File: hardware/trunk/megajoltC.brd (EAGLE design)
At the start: 79.9 x 63 mm, 117 parts, among them IC1 IC_FT230X-SSOP-16, IC2 MCP1826, IC3 MCP1826, J3 JUMPER_CLOSEDTHICK, U1 MCP1700, U11 TLV274, U12 PESDXS4UD, U18 MCP2551SO8, U4 ZXMS6004FF, U8 FAN8303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

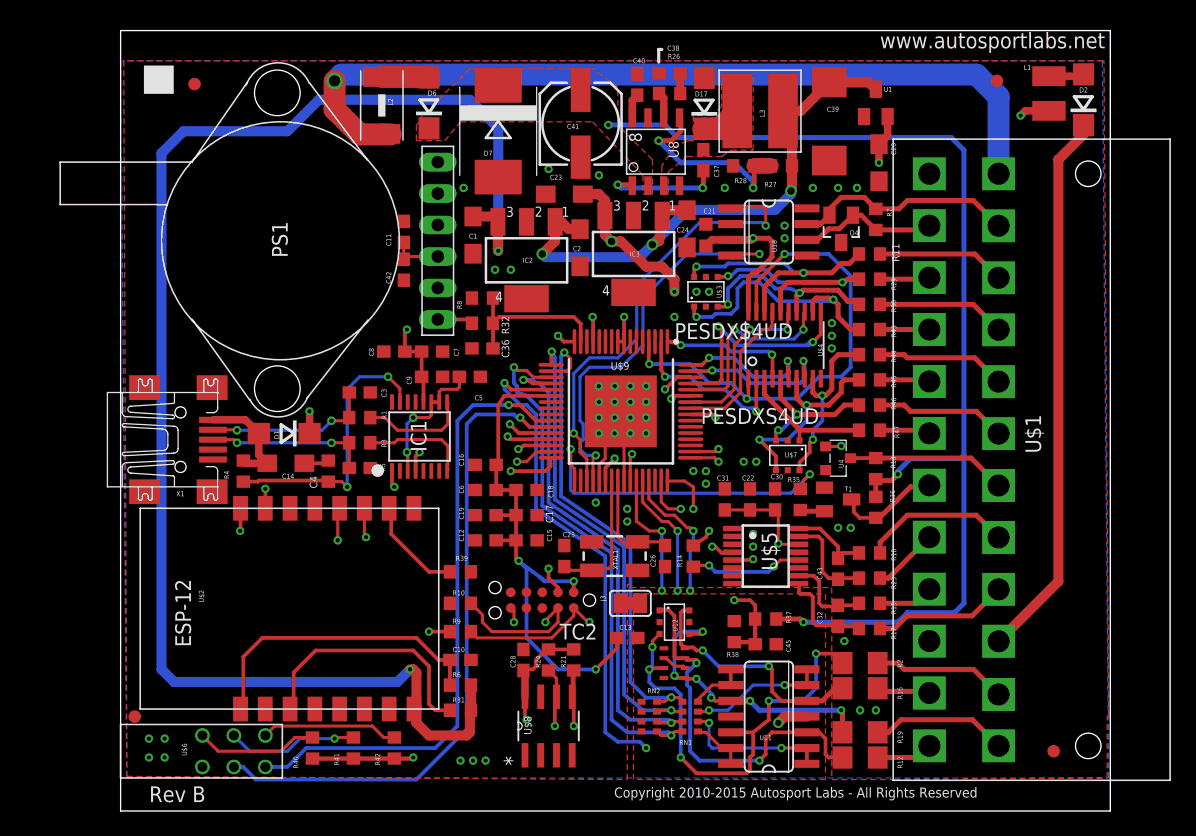
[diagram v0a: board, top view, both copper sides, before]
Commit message: Slight update to routing
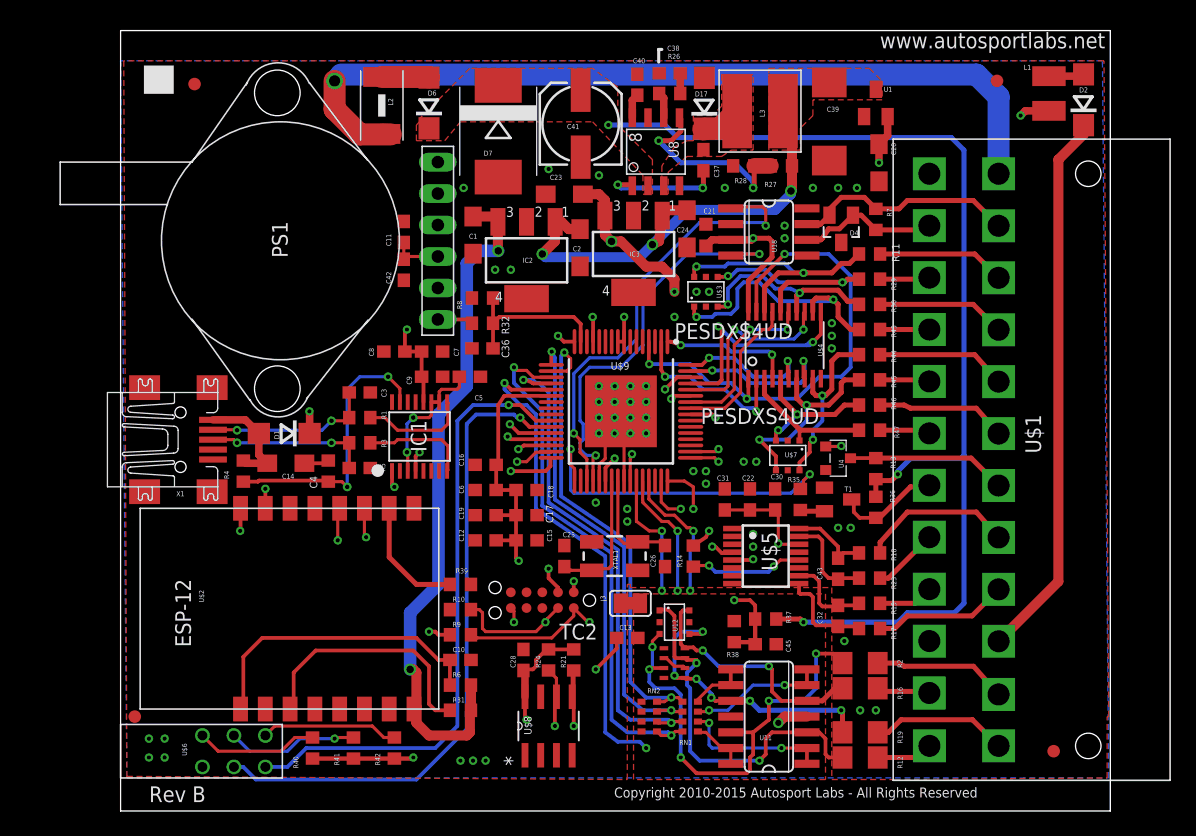
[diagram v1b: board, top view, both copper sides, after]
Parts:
- moved R39 1.02 mm to (27.4, 18.3)
- moved R10 0.51 mm to (27.4, 16.3)
- moved R9 0.25 mm to (27.4, 14.2)
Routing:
- net VCC: track 120.9 -> 56.1 mm
- net +3V3: track 88.5 -> 70.1 mm
- net VDD: track 48.1 -> 39.5 mm
- net SWCLK: track 36.5 -> 34.6 mm
- net N$24: track 8.15 -> 9.76 mm
- added copper zone on layer 1, net VDD

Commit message: Remove R13, minor ground pour changes
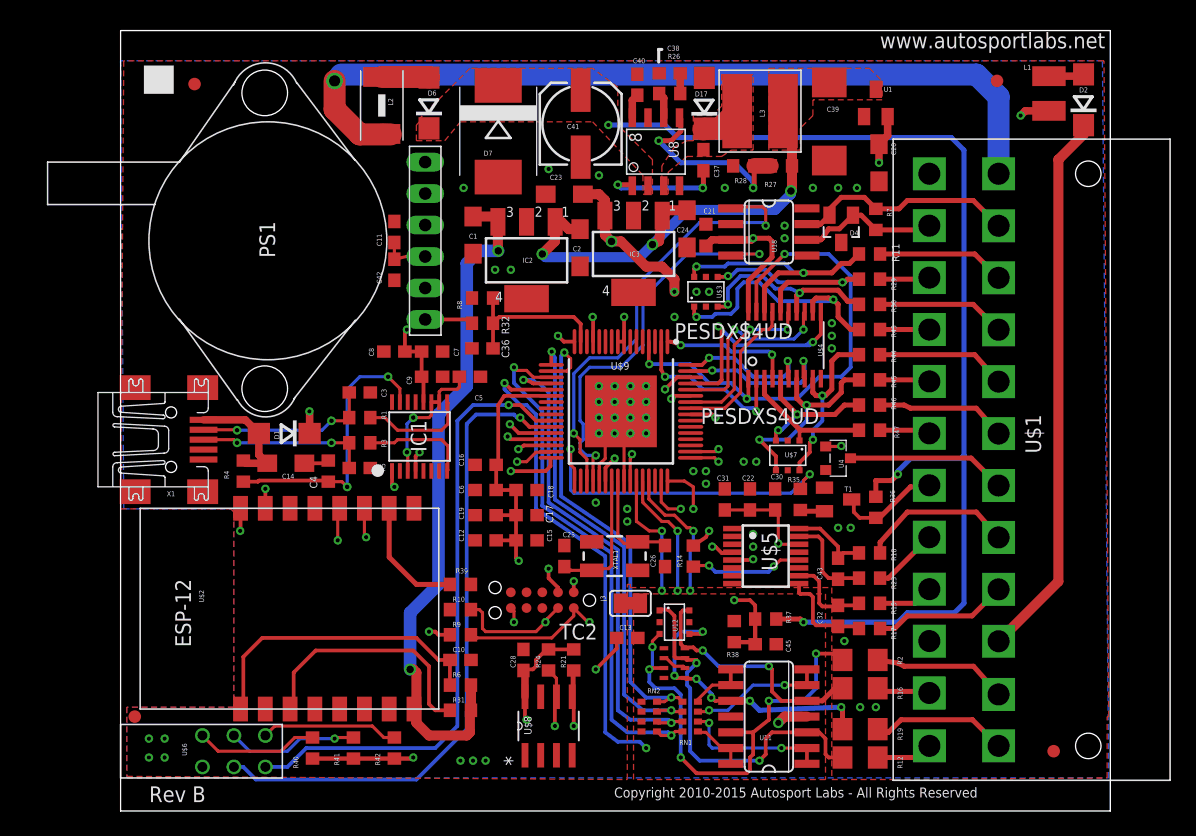
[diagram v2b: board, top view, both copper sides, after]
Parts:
- removed R13: 1K, rcl:R0603
- moved PS1 1.02 mm to (24.6, 46.0)
- moved C11 0.76 mm to (22.1, 46.7)
- moved C42 0.76 mm to (22.1, 43.7)
- moved X1 0.76 mm to (3.17, 30.0)
- moved R19 0.25 mm to (59.7, 6.60)
- moved R2 0.25 mm to (59.7, 12.2)
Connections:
- net PGM_OUT: no longer R13.1
- net SAFE_+12V: no longer R13.2
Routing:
- net N$7: track 2.88 -> 3.90 mm
- net VBUS: track 8.86 -> 9.63 mm
- net FTDI_DP: track 13.1 -> 13.9 mm
- net FTDI_DM: track 13.5 -> 14.2 mm

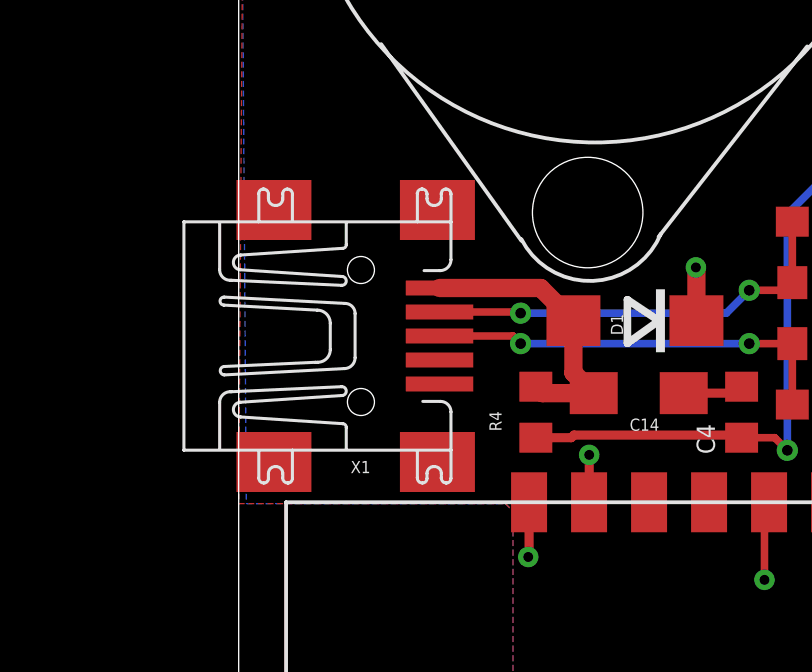
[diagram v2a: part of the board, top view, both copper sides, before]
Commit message: Minor layout trace changes
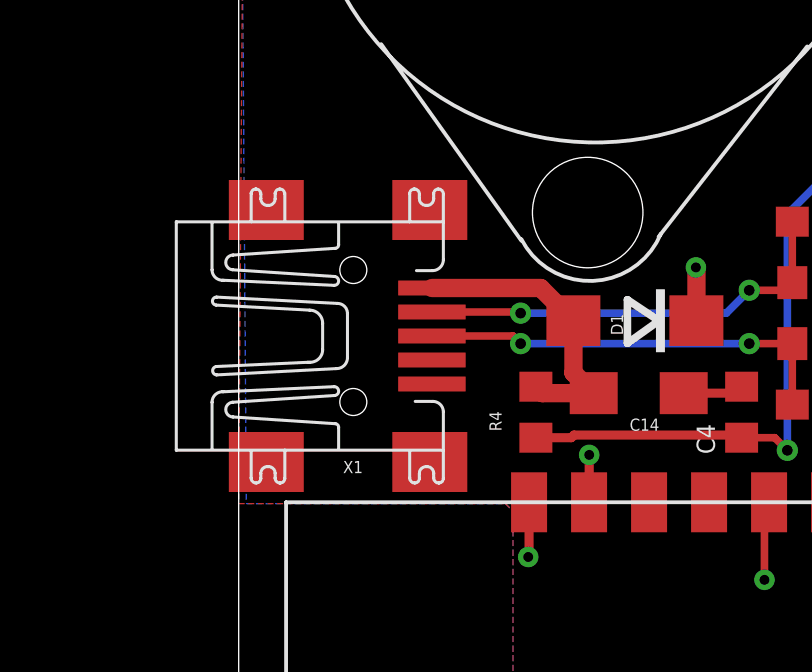
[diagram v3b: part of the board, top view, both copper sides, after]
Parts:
- moved X1 0.25 mm to (2.92, 30.0)
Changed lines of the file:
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@@
 <attribute name="NAME" x="12.811" y="29.999" size="0.4064" layer="25" ratio="10" rot="R90"/>
 </element>
-<element name="X1" library="cnkls_parts" package="MINI-USB_JACK" value="MINI_USB_SHIELD" x="3.175" y="29.972" smashed="yes">
-<attribute name="NAME" x="4.3942" y="25.8064" size="0.4064" layer="25" rot="R180"/>
+<element name="X1" library="cnkls_parts" package="MINI-USB_JACK" value="MINI_USB_SHIELD" x="2.921" y="29.972" smashed="yes">
+<attribute name="NAME" x="4.1402" y="25.8064" size="0.4064" layer="25" rot="R180"/>
 </element>
 <element name="C41" library="rcl" package="153CLV-0605" value="22uF" x="37.1348" y="55.4736" smashed="yes" rot="R90">
@@
 <via x="60.96" y="8.382" extent="1-16" drill="0.3302"/>
 <via x="58.42" y="13.716" extent="1-16" drill="0.3302"/>
-<wire x1="6.695" y1="29.172" x2="6.625" y2="34.172" width="0" layer="19" extent="1-1"/>
+<wire x1="6.441" y1="29.172" x2="6.371" y2="34.172" width="0" layer="19" extent="1-1"/>
 </signal>
 <signal name="+5V">
@@
 <contactref element="X1" pad="1"/>
 <contactref element="R4" pad="2"/>
-<wire x1="6.695" y1="31.572" x2="10.066" y2="31.572" width="0.6096" layer="1"/>
+<wire x1="6.441" y1="31.572" x2="10.066" y2="31.572" width="0.6096" layer="1"/>
 <wire x1="10.066" y1="31.572" x2="11.158" y2="30.48" width="0.6096" layer="1"/>
 <wire x1="11.158" y1="30.48" x2="11.158" y2="28.744" width="0.6096" layer="1"/>
@@
 <contactref element="C3" pad="1"/>
 <wire x1="18.454" y1="33.782" x2="18.454" y2="31.75" width="0.254" layer="1"/>
-<wire x1="6.695" y1="30.772" x2="9.36" y2="30.772" width="0.254" layer="1"/>
+<wire x1="6.441" y1="30.772" x2="9.36" y2="30.772" width="0.254" layer="1"/>
 <wire x1="9.36" y1="30.772" x2="9.398" y2="30.734" width="0.254" layer="1"/>
 <via x="9.398" y="30.734" extent="1-16" drill="0.3556"/>
@@
 <contactref element="C4" pad="1"/>
 <wire x1="18.454" y1="27.686" x2="18.454" y2="29.718" width="0.254" layer="1"/>
-<wire x1="6.695" y1="29.972" x2="9.144" y2="29.972" width="0.254" layer="1"/>
+<wire x1="6.441" y1="29.972" x2="9.144" y2="29.972" width="0.254" layer="1"/>
 <wire x1="9.144" y1="29.972" x2="9.398" y2="29.718" width="0.254" layer="1"/>
 <via x="9.398" y="29.718" extent="1-16" drill="0.3556"/>

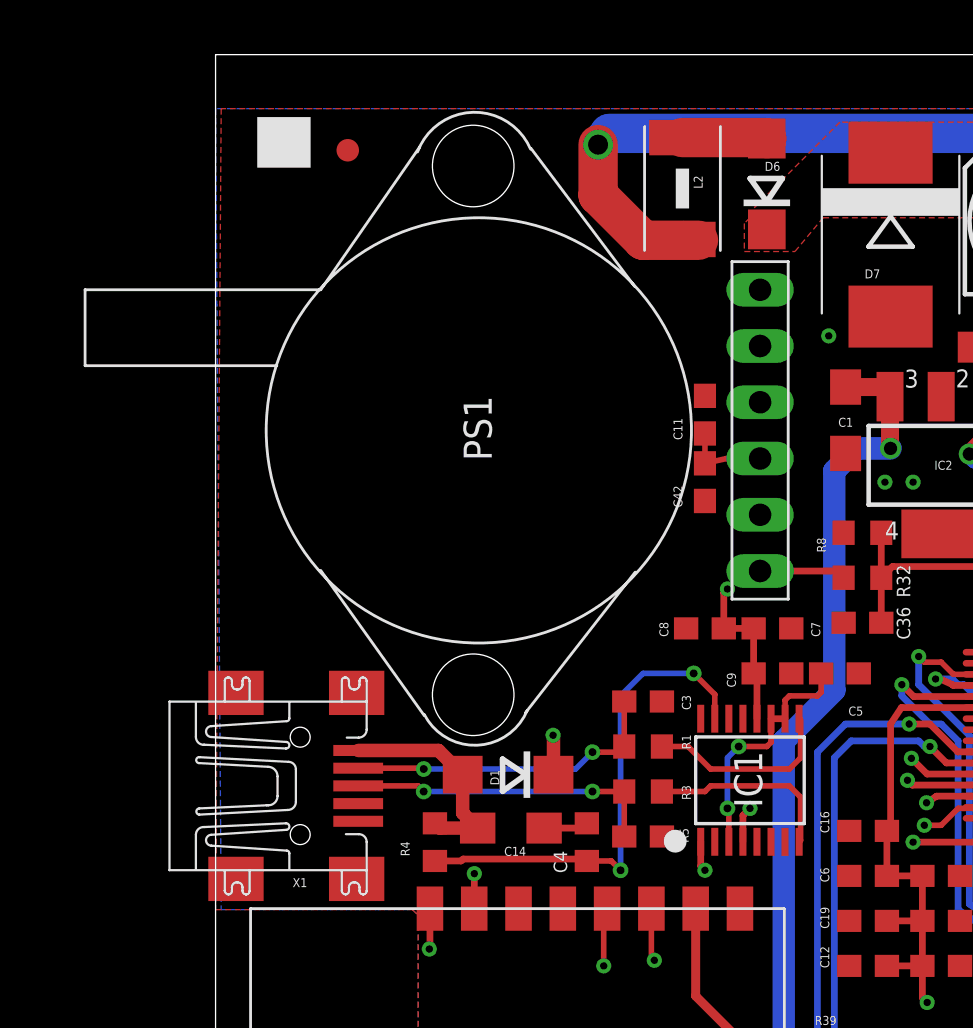
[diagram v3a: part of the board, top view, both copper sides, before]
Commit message: Fix bad ground path issue
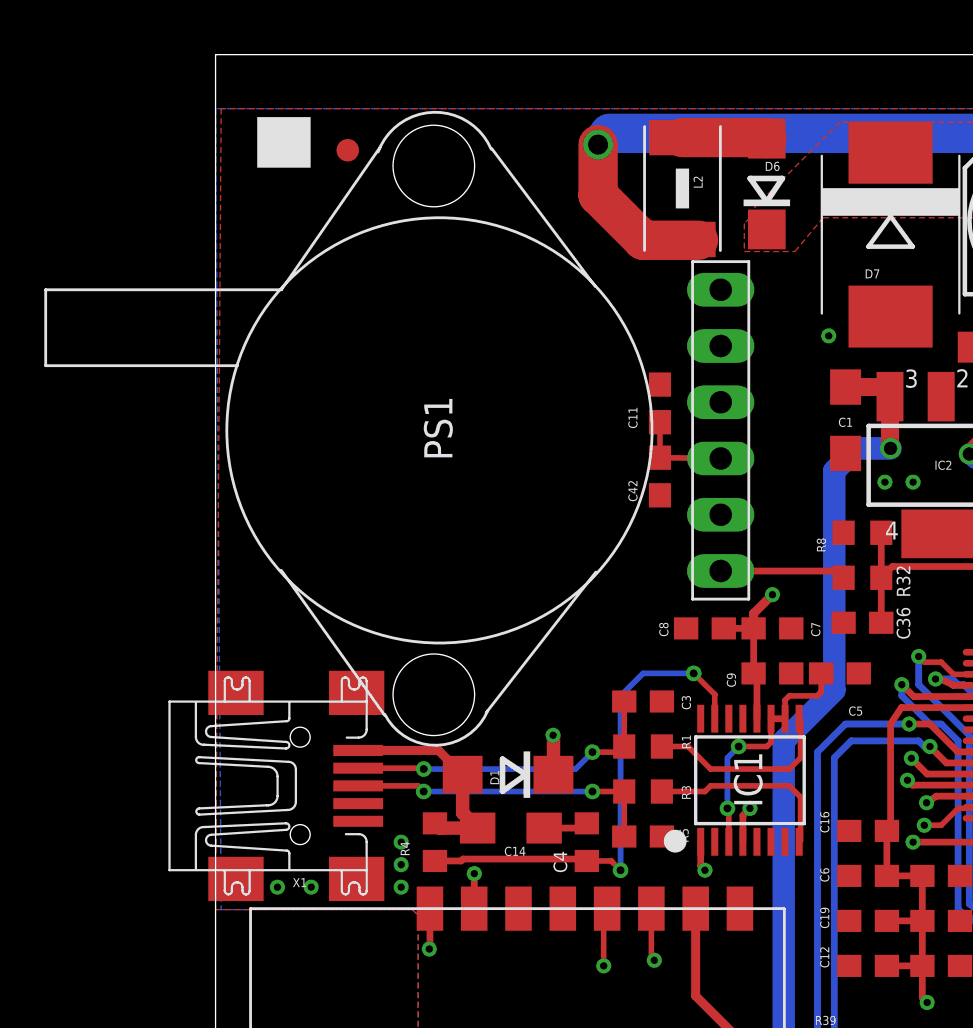
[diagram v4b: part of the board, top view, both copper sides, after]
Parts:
- moved C11 2.09 mm to (20.1, 47.2)
- moved C42 2.05 mm to (20.1, 43.9)
- moved PS1 1.78 mm to (22.8, 46.0)
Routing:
- net N$7: track 3.90 -> 5.68 mm
- net +5V: track 46.0 -> 47.0 mm
- net GND: vias 53 -> 58
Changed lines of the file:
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@@
 <attribute name="NAME" x="58.3694" y="27.6862" size="0.4064" layer="25" rot="R90"/>
 </element>
-<element name="PS1" library="pressure_sensor" package="MPX4250" value="MPX4250" x="24.5872" y="46.0248" smashed="yes" rot="R270">
-<attribute name="NAME" x="12.4714" y="44.6532" size="1.27" layer="25" rot="R90"/>
+<element name="PS1" library="pressure_sensor" package="MPX4250" value="MPX4250" x="22.8092" y="46.0248" smashed="yes" rot="R270">
+<attribute name="NAME" x="10.6934" y="44.6532" size="1.27" layer="25" rot="R90"/>
 </element>
 <element name="R32" library="rcl" package="R0603" value="5.6k" x="29.21" y="39.37" smashed="yes">
@@
 <attribute name="NAME" x="31.369" y="36.576" size="0.6096" layer="25" rot="R90"/>
 </element>
-<element name="C42" library="rcl" package="C0603" value="0.1uf" x="22.098" y="43.688" smashed="yes" rot="R270">
-<attribute name="NAME" x="21.082" y="42.545" size="0.4064" layer="25" rot="R90"/>
+<element name="C42" library="rcl" package="C0603" value="0.1uf" x="20.066" y="43.942" smashed="yes" rot="R270">
+<attribute name="NAME" x="19.05" y="42.799" size="0.4064" layer="25" rot="R90"/>
 </element>
 <element name="T1" library="transistor" package="SOT23-EBC" value="" x="57.912" y="25.146" smashed="yes" rot="R270">
@@
 <attribute name="VALUE" x="59.563" y="28.702" size="1.27" layer="27"/>
 </element>
-<element name="C11" library="rcl" package="C0603" value="0.1uf" x="22.098" y="46.736" smashed="yes" rot="R90">
-<attribute name="NAME" x="21.082" y="45.593" size="0.4064" layer="25" rot="R90"/>
-<attribute name="VALUE" x="24.13" y="45.847" size="1.27" layer="27" rot="R90"/>
+<element name="C11" library="rcl" package="C0603" value="0.1uf" x="20.066" y="47.244" smashed="yes" rot="R90">
+<attribute name="NAME" x="19.05" y="46.101" size="0.4064" layer="25" rot="R90"/>
+<attribute name="VALUE" x="22.098" y="46.355" size="1.27" layer="27" rot="R90"/>
 </element>
 <element name="C6" library="resistor" package="C0603" value="4.7uF" x="29.464" y="25.908" smashed="yes" rot="R180">
@@
 <via x="60.96" y="8.382" extent="1-16" drill="0.3302"/>
 <via x="58.42" y="13.716" extent="1-16" drill="0.3302"/>
-<wire x1="6.441" y1="29.172" x2="6.371" y2="34.172" width="0" layer="19" extent="1-1"/>
+<via x="2.794" y="25.4" extent="1-16" drill="0.3302"/>
+<via x="4.318" y="25.4" extent="1-16" drill="0.3302"/>
+<via x="8.382" y="25.4" extent="1-16" drill="0.3302"/>
+<via x="8.382" y="26.416" extent="1-16" drill="0.3302"/>
+<via x="8.382" y="27.432" extent="1-16" drill="0.3302"/>
 </signal>
 <signal name="+5V">
@@
 <contactref element="C23" pad="+"/>
 <contactref element="L1" pad="1"/>
-<wire x1="24.5872" y1="44.7548" x2="23.0768" y2="44.7548" width="0.254" layer="1"/>
-<wire x1="23.0768" y1="44.7548" x2="22.098" y2="44.538" width="0.254" layer="1"/>
-<wire x1="22.098" y1="44.538" x2="22.098" y2="45.886" width="0.254" layer="1"/>
+<wire x1="22.8092" y1="44.7548" x2="23.0768" y2="44.7548" width="0.254" layer="1"/>
+<wire x1="23.0768" y1="44.7548" x2="20.066" y2="44.792" width="0.254" layer="1"/>
+<wire x1="20.066" y1="44.792" x2="20.066" y2="46.394" width="0.254" layer="1"/>
 <wire x1="39.0906" y1="48.0568" x2="39.0906" y2="49.3014" width="0.8128" layer="1"/>
 <wire x1="39.0906" y1="49.3014" x2="38.608" y2="49.784" width="0.8128" layer="1"/>
@@
 <contactref element="X1" pad="1"/>
 <contactref element="R4" pad="2"/>
-<wire x1="6.441" y1="31.572" x2="10.066" y2="31.572" width="0.6096" layer="1"/>
-<wire x1="10.066" y1="31.572" x2="11.158" y2="30.48" width="0.6096" layer="1"/>
+<wire x1="6.441" y1="31.572" x2="10.066" y2="31.572" width="0.4064" layer="1"/>
+<wire x1="10.066" y1="31.572" x2="11.158" y2="30.48" width="0.4064" layer="1"/>
 <wire x1="11.158" y1="30.48" x2="11.158" y2="28.744" width="0.6096" layer="1"/>
 <wire x1="11.158" y1="28.744" x2="11.835" y2="28.067" width="0.6096" layer="1"/>
@@
 <contactref element="PS1" pad="OUT"/>
 <contactref element="R32" pad="1"/>
-<wire x1="24.5872" y1="39.6748" x2="28.0552" y2="39.6748" width="0.3048" layer="1"/>
+<wire x1="22.8092" y1="39.6748" x2="28.0552" y2="39.6748" width="0.3048" layer="1"/>
 <wire x1="28.0552" y1="39.6748" x2="28.36" y2="39.37" width="0.3048" layer="1"/>
 </signal>
@@
 <wire x1="24.447" y1="33.005" x2="24.447" y2="34.989" width="0.3048" layer="1"/>
 <wire x1="24.447" y1="34.989" x2="24.384" y2="35.052" width="0.3048" layer="1"/>
-<via x="23.114" y="38.862" extent="1-16" drill="0.3302"/>
-<wire x1="22.948" y1="37.084" x2="22.948" y2="38.696" width="0.3048" layer="1"/>
-<wire x1="22.948" y1="38.696" x2="23.114" y2="38.862" width="0.3048" layer="1"/>
 <wire x1="26.582" y1="14.224" x2="25.654" y2="14.224" width="0.3048" layer="1"/>
 <wire x1="25.654" y1="14.224" x2="25.4" y2="14.478" width="0.3048" layer="1"/>
@@
 <wire x1="38.354" y1="11.43" x2="40.044" y2="13.12" width="0.3048" layer="1"/>
 <via x="38.354" y="11.43" extent="1-16" drill="0.3302"/>
+<via x="25.146" y="38.608" extent="1-16" drill="0.3302"/>
+<wire x1="24.296" y1="37.084" x2="24.296" y2="37.758" width="0.4064" layer="1"/>
+<wire x1="24.296" y1="37.758" x2="25.146" y2="38.608" width="0.4064" layer="1"/>
 </signal>
 <signal name="FTDI_DM">
